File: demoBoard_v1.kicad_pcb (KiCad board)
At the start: 2 copper layers, 100 x 100 mm, 47 parts, among them P1 SPI_Header, P10 RTC_Serial, P11 WD_Header, P12 WD_1.2V_NC, P13 RTC_Aux, P14 Flash_3v3_NC, P15 WD_SENSE_3.3V_NC, P2 3x_CS_Header, P3 Power_Header, P4 LOAD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

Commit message: Cleaned up and made the board smaller. Began adding silkscreen
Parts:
- moved R4 46.0 mm to (215.9, 68.5), turned to 270 degrees
- moved D1 35.7 mm to (216.0, 76.0), turned to 0 degrees
- moved R6 34.2 mm to (228.0, 109.0)
- moved Q3 31.3 mm to (216.0, 87.0)
- moved R3 29.8 mm to (231.0, 124.0), turned to 0 degrees
- moved P7 29.2 mm to (211.0, 112.0)
- moved Q4 29.1 mm to (216.0, 98.0)
- moved P5 28.8 mm to (211.0, 123.0), turned to 90 degrees
- moved R7 25.3 mm to (218.0, 109.0)
- moved R5 25.2 mm to (223.0, 109.0), turned to 180 degrees
- moved Q1 22.4 mm to (237.0, 122.0)
- moved P4 22.1 mm to (211.0, 134.8), turned to 270 degrees
- moved D2 20.4 mm to (216.0, 104.0)
- moved RShunt1 14.1 mm to (223.0, 124.0), turned to 180 degrees
- moved RLimit1 13.5 mm to (223.0, 141.0)
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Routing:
- net +1V2: track 122.2 -> 94.8 mm, vias 3 -> 1
- net +3V3: track 262.3 -> 236.0 mm, vias 4 -> 2
- net INA_Supply: track 34.8 -> 55.1 mm, vias 0 -> 2
- net INA_Alert: track 53.7 -> 38.3 mm, vias 4 -> 2
- net Net-(D2-Pad2): track 2.95 -> 11.6 mm
- net Net-(D1-Pad1): track 16.0 -> 10.3 mm
- net Net-(D1-Pad2): track 2.79 -> 8.32 mm
- net Load+: track 20.8 -> 25.7 mm, vias 0 -> 1
- net Net-(RLimit1-Pad1): track 10.3 -> 5.89 mm, vias 2 -> 0
- net INA_Out: track 21.3 -> 25.5 mm
- net Net-(D2-Pad1): track 9.57 -> 11.3 mm
- net INA_GND: track 73.8 -> 72.3 mm, vias 3 -> 0
- net GND: track 43.3 -> 41.9 mm
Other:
- board text added: "+Load -Load"
- board text added: "3v3 COM Ext"
- board text added: "Alert Out"
- board text added: "CS1 CS2 CS3"
- board text added: "Ext COM GND"
- board text added: "INA_GND"
- board text added: "INA_Signal"
- board text added: "Load"
- board text added: "MOSI MISO CLK"

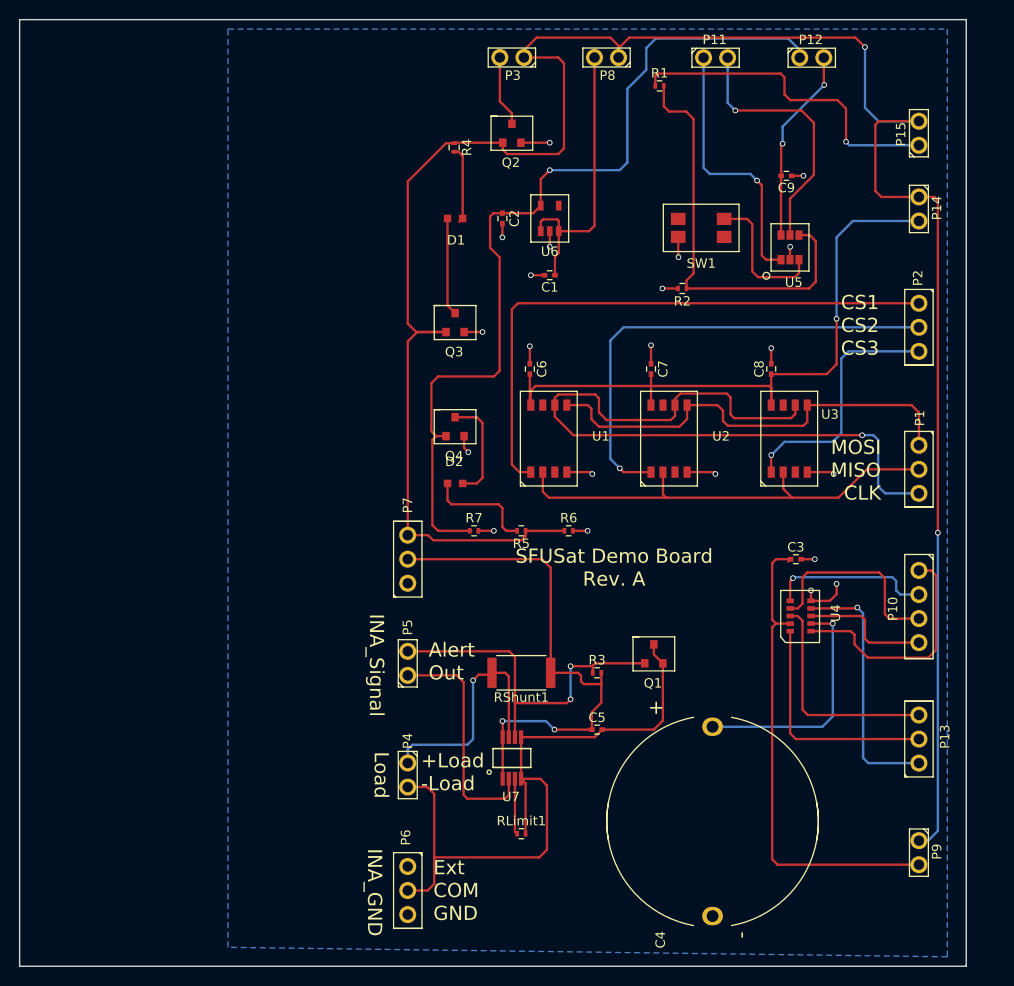
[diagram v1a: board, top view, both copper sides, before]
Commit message: Added separate ground pane for SEL monitor to facilitate independent testing of it. Beefed up power tracks. Discovered error with external load connection being shorted to ground at the connector, and through the FET source, rendering the FET useless. Will fix schematic in next commit. Todo: TVS, add LED for SEL monitor, silkscreen, mount holes, beef up 3.3V power lines.
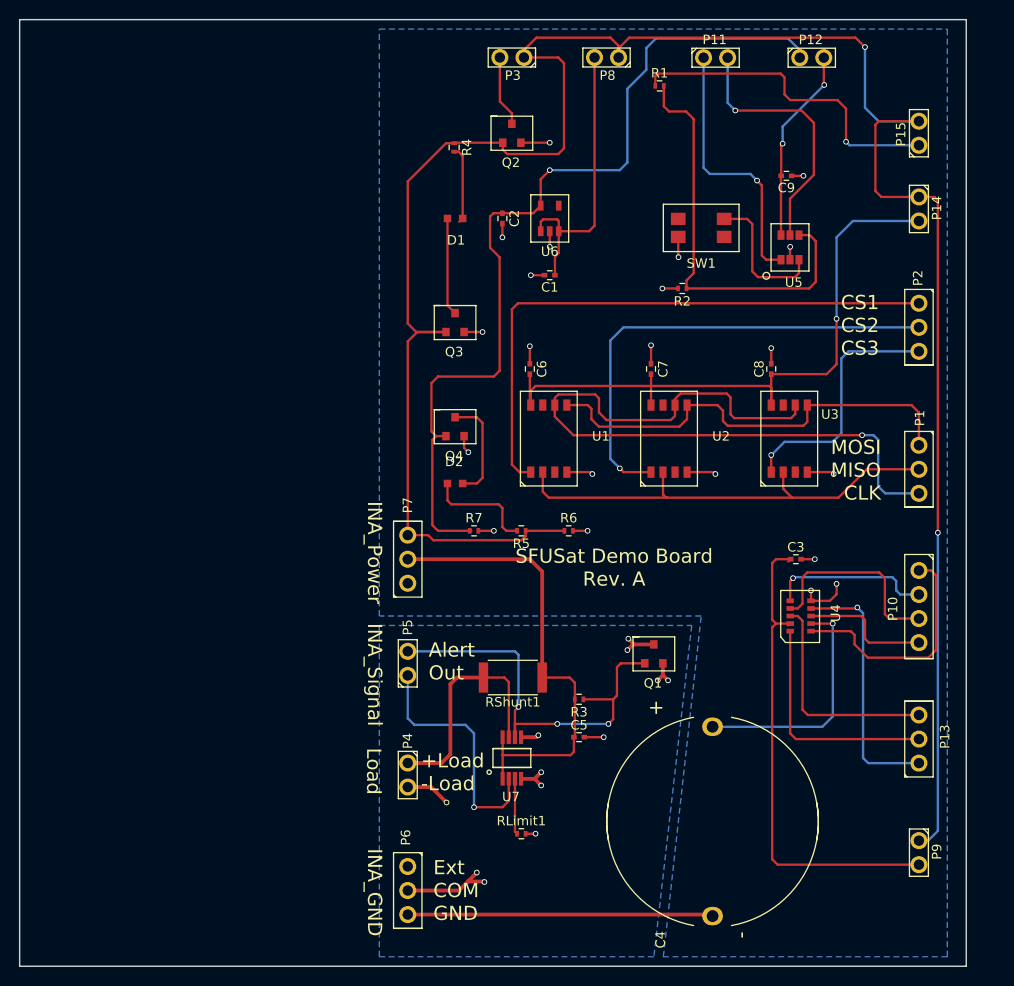
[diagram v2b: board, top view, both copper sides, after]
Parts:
- moved R3 3.38 mm to (229.1, 126.8), turned to 180 degrees
- moved C5 2.06 mm to (229.1, 130.8)
- moved RShunt1 1.03 mm to (222.1, 124.5)
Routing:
- net INA_GND: track 72.3 -> 29.7 mm, vias 0 -> 12
- net GND: track 41.9 -> 74.2 mm
- net INA_Alert: track 38.3 -> 44.7 mm, vias 2 -> 3
- net INA_Supply: track 55.1 -> 49.0 mm, vias 2 -> 0
- net INA_Out: track 25.5 -> 26.8 mm, vias 0 -> 1
- net Load+: track 25.7 -> 25.1 mm, vias 1 -> 0
- added copper zone on B.Cu, net INA_GND
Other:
- board text added: "INA_Power"

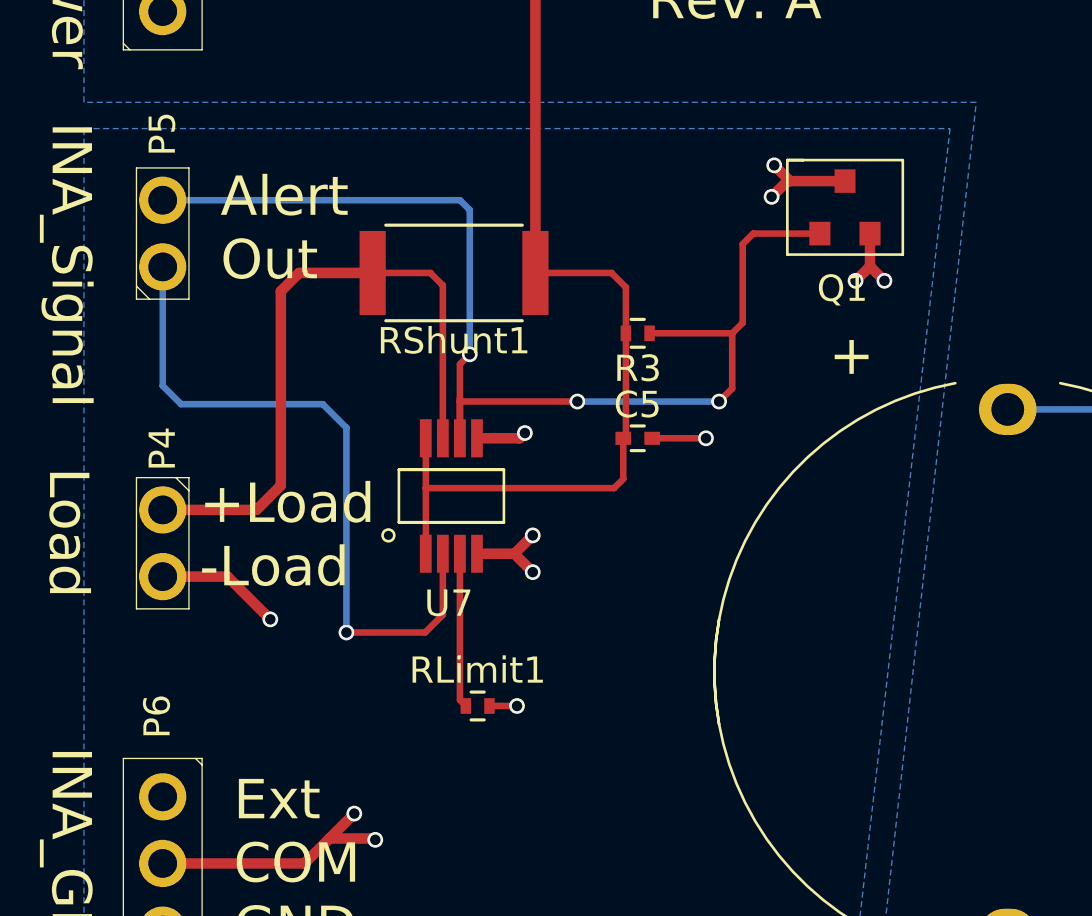
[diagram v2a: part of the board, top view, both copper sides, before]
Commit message: Fixed SEL monitor mistake ground connection
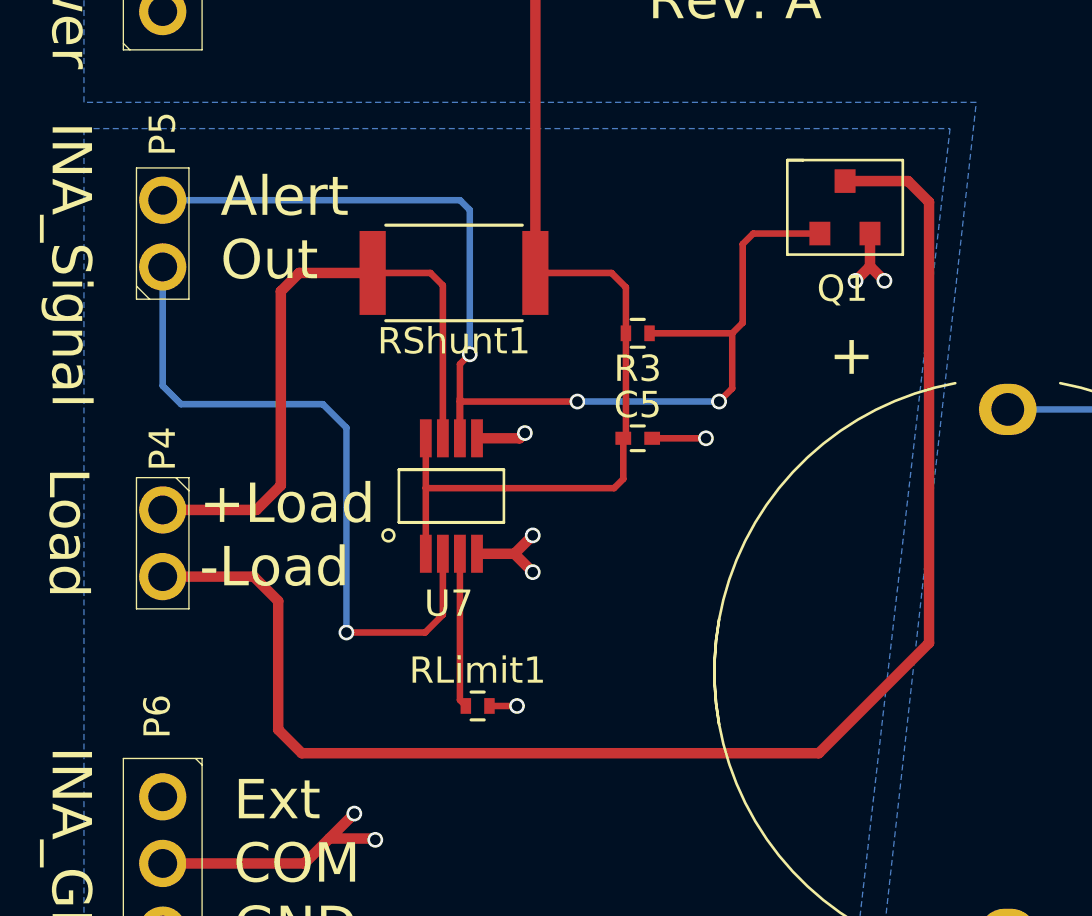
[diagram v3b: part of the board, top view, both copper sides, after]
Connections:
- P4 pad 2: INA_GND -> Load-
- Q1 pad 1: INA_GND -> Load-
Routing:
- net Load-: track 0.00 -> 56.9 mm
- net INA_GND: track 29.7 -> 21.1 mm, vias 12 -> 9
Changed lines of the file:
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@@
 (kicad_pcb (version 4) (host pcbnew 4.0.4-stable)
   (general
-    (links 98)
+    (links 97)
     (no_connects 0)
     (area 169.924999 54.924999 270.075001 155.075001)
@@
     (zones 0)
     (modules 47)
-    (nets 49)
+    (nets 50)
   )
   (page A4)
@@
   )
   (setup
-    (last_trace_width 0.25)
+    (last_trace_width 0.4)
     (user_trace_width 0.254)
     (user_trace_width 0.4)
@@
   (net 47 "Net-(U3-Pad7)")
   (net 48 "Net-(U6-Pad4)")
+  (net 49 Load-)
   (net_class Default "This is the default net class."
     (clearance 0.2)
@@
     (add_net INA_Supply)
     (add_net Load+)
+    (add_net Load-)
     (add_net "Net-(C1-Pad1)")
     (add_net "Net-(C3-Pad1)")
@@
     (fp_line (start -2.5 -1) (end 2.5 -1) (layer F.SilkS) (width 0.05))
     (pad 2 thru_hole circle (at 1.27 0 270) (size 1.8 1.8) (drill 1.1) (layers *.Cu *.Mask)
-      (net 7 INA_GND))
+      (net 49 Load-))
     (pad 1 thru_hole circle (at -1.27 0 270) (size 1.8 1.8) (drill 1.1) (layers *.Cu *.Mask)
       (net 22 Load+))
@@
     (fp_line (start -2.2 1.8) (end -2.2 -1.8) (layer F.SilkS) (width 0.1))
     (pad 1 smd rect (at 0 -1) (size 0.8 0.9) (layers F.Cu F.Paste F.Mask)
-      (net 7 INA_GND))
+      (net 49 Load-))
     (pad 2 smd rect (at -0.96 1) (size 0.8 0.9) (layers F.Cu F.Paste F.Mask)
       (net 23 INA_Alert))
@@
   (segment (start 216.4 147) (end 217.35 146.05) (width 0.4) (layer F.Cu) (net 7))
   (segment (start 217.35 146.05) (end 218.3 145.1) (width 0.4) (layer F.Cu) (net 7))
-  (segment (start 211 136.07) (end 213.47 136.07) (width 0.4) (layer F.Cu) (net 7))
-  (via (at 215.1 137.7) (size 0.6) (drill 0.4) (layers F.Cu B.Cu) (net 7))
-  (segment (start 213.47 136.07) (end 215.1 137.7) (width 0.4) (layer F.Cu) (net 7))
   (segment (start 237.95 124.25) (end 238.5 124.8) (width 0.4) (layer F.Cu) (net 7))
   (via (at 238.5 124.8) (size 0.6) (drill 0.4) (layers F.Cu B.Cu) (net 7))
@@
   (via (at 237.4 124.8) (size 0.6) (drill 0.4) (layers F.Cu B.Cu) (net 7))
   (segment (start 237.95 124.25) (end 237.4 124.8) (width 0.4) (layer F.Cu) (net 7))
-  (segment (start 234.9 121) (end 234.8 121) (width 0.4) (layer F.Cu) (net 7))
-  (via (at 234.2 121.6) (size 0.6) (drill 0.4) (layers F.Cu B.Cu) (net 7))
-  (segment (start 234.8 121) (end 234.2 121.6) (width 0.4) (layer F.Cu) (net 7))
-  (segment (start 237 121) (end 234.9 121) (width 0.4) (layer F.Cu) (net 7))
-  (via (at 234.3 120.4) (size 0.6) (drill 0.4) (layers F.Cu B.Cu) (net 7))
-  (segment (start 234.9 121) (end 234.3 120.4) (width 0.4) (layer F.Cu) (net 7))
   (segment (start 222.975 130.8) (end 224.6 130.8) (width 0.4) (layer F.Cu) (net 7))
   (via (at 224.8 130.6) (size 0.6) (drill 0.4) (layers F.Cu B.Cu) (net 7))
@@
   (segment (start 247.4 76.6) (end 247.4 81.6) (width 0.25) (layer F.Cu) (net 40))
   (segment (start 246.85 76.05) (end 247.4 76.6) (width 0.25) (layer F.Cu) (net 40))
+  (segment (start 211 136.07) (end 214.47 136.07) (width 0.4) (layer F.Cu) (net 49) (status 400000))
+  (segment (start 239.4 121) (end 237 121) (width 0.4) (layer F.Cu) (net 49) (status 800000))
+  (segment (start 240.2 121.8) (end 239.4 121) (width 0.4) (layer F.Cu) (net 49))
+  (segment (start 240.2 138.6) (end 240.2 121.8) (width 0.4) (layer F.Cu) (net 49))
+  (segment (start 236 142.8) (end 240.2 138.6) (width 0.4) (layer F.Cu) (net 49))
+  (segment (start 216.3 142.8) (end 236 142.8) (width 0.4) (layer F.Cu) (net 49))
+  (segment (start 215.4 141.9) (end 216.3 142.8) (width 0.4) (layer F.Cu) (net 49))
+  (segment (start 215.4 137) (end 215.4 141.9) (width 0.4) (layer F.Cu) (net 49))
+  (segment (start 214.47 136.07) (end 215.4 137) (width 0.4) (layer F.Cu) (net 49))
   (zone (net 2) (net_name GND) (layer B.Cu) (hatch edge 0.508)
     (connect_pads (clearance 0.508))

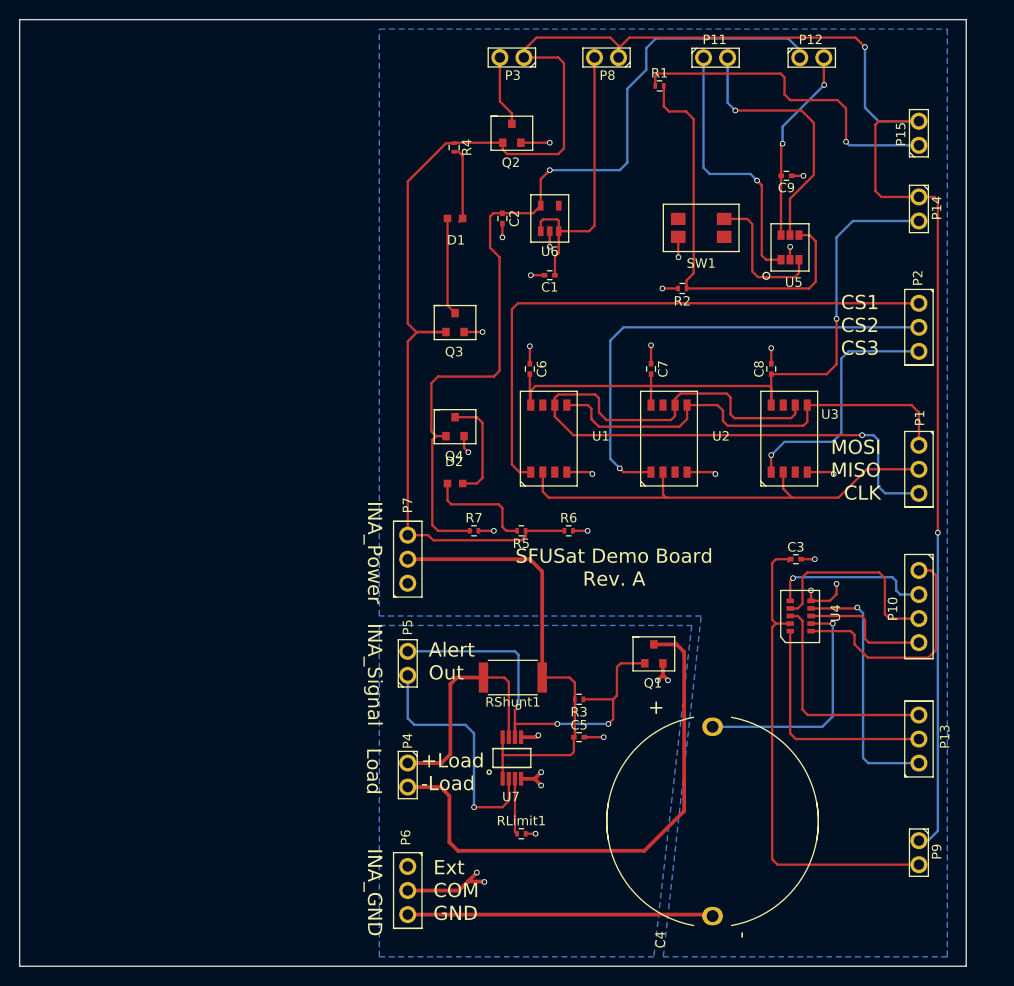
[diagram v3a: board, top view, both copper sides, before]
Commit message: Added more silkscreens including the logo. Reorganized some traces
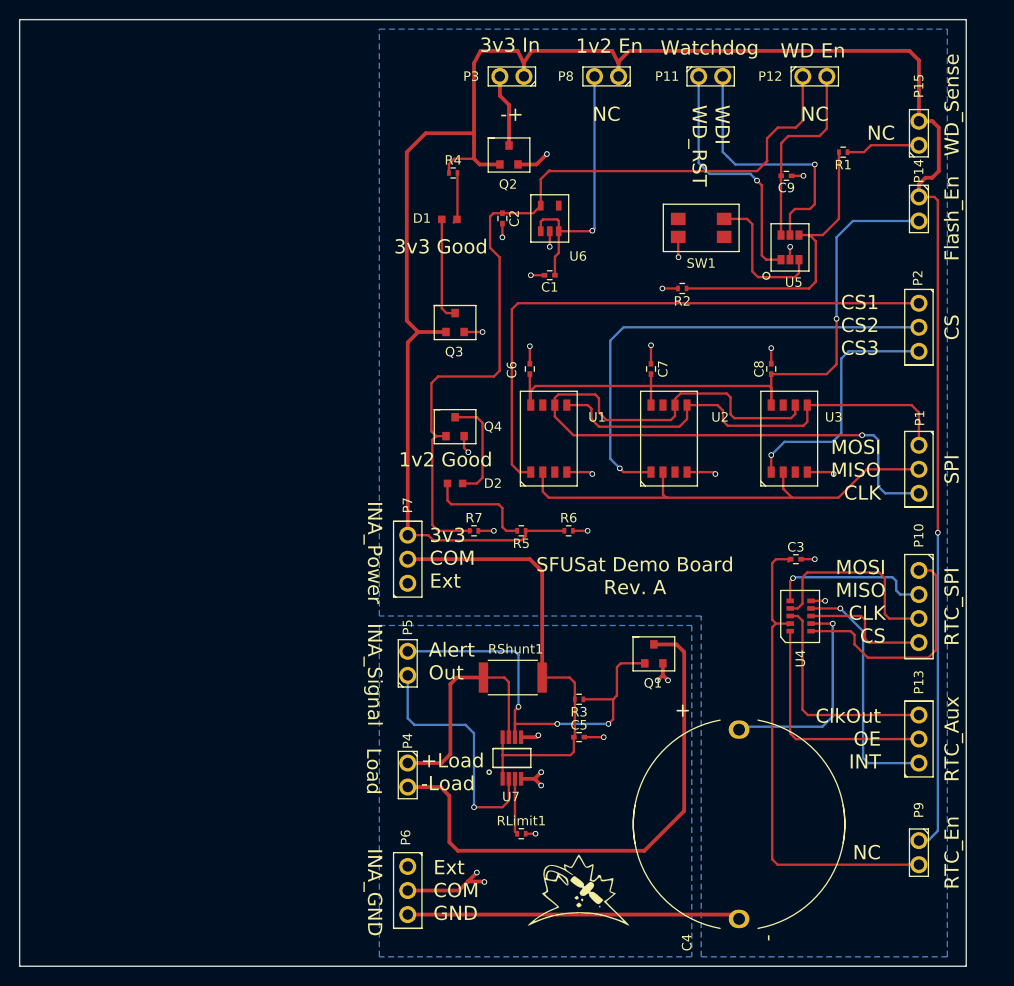
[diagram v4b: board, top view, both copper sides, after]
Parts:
- added G***: LOGO, Graphics:SFUSat_15mm_2, F.Cu at (229.0, 147.0)
- moved R1 20.6 mm to (257.0, 69.0), turned to 180 degrees
- moved C4 2.82 mm to (246.0, 140.0)
- moved R4 2.70 mm to (215.8, 71.2), turned to 0 degrees
- moved Q2 2.32 mm to (221.7, 69.3)
- moved P11 2.05 mm to (243.0, 61.0)
- moved P12 2.01 mm to (254.0, 61.0)
- moved P3 2.00 mm to (222.0, 61.0)
- moved P8 2.00 mm to (232.0, 61.0)
- moved D1 0.61 mm to (215.4, 76.1)
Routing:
- net Net-(P15-Pad1): track 35.2 -> 7.85 mm, vias 1 -> 0
- net Net-(R1-Pad2): track 44.3 -> 31.1 mm
- net +3V3: track 236.0 -> 230.1 mm, vias 2 -> 1
- net +1V2: track 94.8 -> 91.6 mm, vias 1 -> 0
- net Net-(D1-Pad2): track 8.32 -> 5.42 mm
- net Net-(C4-Pad1): track 25.3 -> 22.6 mm
- net Net-(C1-Pad1): track 30.8 -> 28.9 mm, vias 0 -> 1
- net WD_RESET: track 28.2 -> 26.4 mm
- net RTC_INT: track 27.2 -> 26.0 mm
- net Net-(D1-Pad1): track 10.3 -> 11.0 mm
- net GND: track 74.2 -> 73.8 mm, vias 21 -> 20
- net Net-(C9-Pad2): vias 2 -> 0
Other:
- board text added: "-+"
- board text added: "1v2 En"
- board text added: "1v2 Good"
- board text added: "3v3 Good"
- board text added: "3v3 In"
- board text added: "CS"
- board text added: "ClkOut OE INT"
- board text added: "Flash_En"
- board text added: "MOSI MISO CLK CS"
- board text added: "NC"
- board text added: "RTC_Aux"
- board text added: "RTC_En"
- board text added: "RTC_SPI"
- board text added: "SPI"
- board text added: "WD En"
- board text added: "WDI WD_RST"
- board text added: "WD_Sense"
- board text added: "Watchdog"

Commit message: Ready to be sent to board house
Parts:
- added D3: PESD5Zx, SFUSat:PESD57zx, F.Cu at (228.3, 68.1)
- added D4: PESD5Zx, SFUSat:PESD57zx, F.Cu at (230.0, 121.0)
- added D5: Led_Small, SFUSat:LED_150060GS75000, F.Cu at (236.1, 128.9)
- added Q5: DMN2075U, SFUSat:SOT23_DMN2075U, F.Cu at (229.0, 139.3)
- added R10: 0, Resistors_SMD:R_0402, F.Cu at (223.4, 146.7)
- added R8: 220, Resistors_SMD:R_0402, F.Cu at (234.1, 132.9)
- added R9: 10k, Resistors_SMD:R_0402, F.Cu at (227.7, 135.1)
- C5, C6, C7, C8, C9: value 1µF -> 0.1µF
- moved G*** 3.20 mm to (230.1, 150.0)
- moved P13 2.00 mm to (265.0, 133.0)
- moved P14 2.00 mm to (265.0, 77.0)
- moved P9 2.00 mm to (265.0, 145.0)
- moved R7 1.20 mm to (219.2, 109.0)
- moved P10 1.00 mm to (265.0, 118.0)
- moved P11 1.00 mm to (242.0, 61.0)
- moved P5 1.00 mm to (211.0, 124.0)
- moved P6 1.00 mm to (211.0, 146.0)
- moved RShunt1 0.90 mm to (223.0, 124.5)
- moved P4 0.80 mm to (211.0, 134.0)
- moved P1 0.50 mm to (265.0, 103.0)
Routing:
- net Net-(R10-Pad1): track 0.00 -> 23.8 mm, vias 0 -> 2
- net INA_Supply: track 49.0 -> 69.8 mm, vias 0 -> 2
- net INA_Alert: track 44.7 -> 65.2 mm, vias 3 -> 4
- net Net-(D5-Pad1): track 0.00 -> 14.1 mm
- net +3V3: track 230.1 -> 238.3 mm, vias 1 -> 0
- net Net-(D5-Pad2): track 0.00 -> 6.12 mm
- net RTC_INT: track 26.0 -> 29.3 mm
- net RTC_SCL: track 21.4 -> 18.2 mm
- net GND: track 73.8 -> 76.7 mm, vias 20 -> 21
- net RTC_MOSI: track 25.2 -> 27.3 mm
- net CLKOut: track 24.1 -> 26.0 mm
- net WD_RESET: track 26.4 -> 28.3 mm
- net RTC_OE: track 24.6 -> 26.5 mm
- net Net-(C3-Pad1): track 51.6 -> 53.4 mm
- net WDI: track 27.7 -> 29.0 mm
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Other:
- board size 100 x 100 mm -> 68 x 100 mm
- board text added: "+"
- board text added: "0Ω"
- board text added: "1"
- board text added: "Load Power"
- board text added: "RESET"
